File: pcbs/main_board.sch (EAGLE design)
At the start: 56 parts, among them IC1 317T, IC2 MEGA48/88/168-AU, J1 22-27-2021-02, K1 G6K-2F, Q1 MOSFET-NCHANNELSMD, Q2 MOSFET-NCHANNELSMD

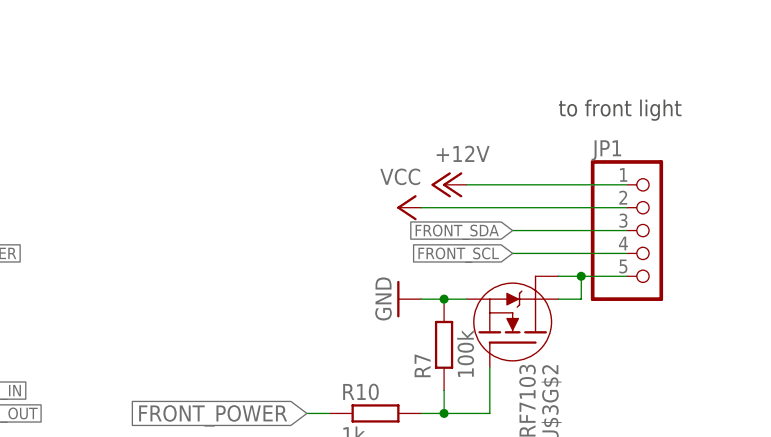
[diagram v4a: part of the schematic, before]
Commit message: Main Board: added i2c pullups.
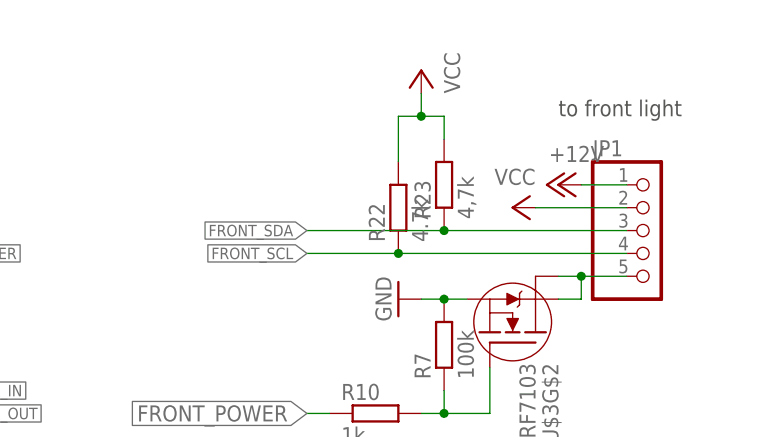
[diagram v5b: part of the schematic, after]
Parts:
- added R22: 4.7k, resistor:R-EU_R0805
- added R23: 4,7k, resistor:R-EU_R0805
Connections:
- net FRONT_SCL: now also R22.1
- net FRONT_SDA: now also R23.1
- net VCC: now also R22.2, R23.2
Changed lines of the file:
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@@
 <part name="R21" library="resistor" deviceset="R-EU_" device="R0805" value="1k"/>
 <part name="U$4" library="ShortCircuitRobotics" deviceset="IRF7413" device=""/>
+<part name="R22" library="resistor" deviceset="R-EU_" device="R0805" value="4.7k"/>
+<part name="R23" library="resistor" deviceset="R-EU_" device="R0805" value="4,7k"/>
+<part name="P+14" library="supply1" deviceset="VCC" device=""/>
 </parts>
 <sheets>
@@
 <instance part="JP2" gate="A" x="490.22" y="78.74"/>
 <instance part="GND6" gate="1" x="462.28" y="76.2" rot="R270"/>
-<instance part="P+5" gate="1" x="480.06" y="149.86" rot="MR270"/>
+<instance part="P+5" gate="1" x="492.76" y="149.86" rot="MR270"/>
 <instance part="P+6" gate="1" x="53.34" y="91.44"/>
 <instance part="Q1" gate="G$1" x="53.34" y="66.04"/>
@@
 <instance part="R10" gate="G$1" x="472.44" y="124.46"/>
 <instance part="P+8" gate="1" x="472.44" y="83.82" rot="MR270"/>
-<instance part="P+9" gate="VCC" x="474.98" y="147.32" rot="MR270"/>
+<instance part="P+9" gate="VCC" x="487.68" y="147.32" rot="MR270"/>
 <instance part="JP3" gate="G$1" x="439.42" y="99.06"/>
 <instance part="P+10" gate="VCC" x="454.66" y="101.6" rot="MR90"/>
@@
 <instance part="R21" gate="G$1" x="469.9" y="25.4"/>
 <instance part="U$4" gate="G$1" x="485.14" y="38.1" rot="MR90"/>
+<instance part="R22" gate="G$1" x="474.98" y="147.32" rot="R90"/>
+<instance part="R23" gate="G$1" x="480.06" y="149.86" rot="R90"/>
+<instance part="P+14" gate="VCC" x="477.52" y="162.56" rot="MR0"/>
 </instances>
 <busses>
@@
 <pinref part="JP1" gate="A" pin="1"/>
 <pinref part="P+5" gate="1" pin="+12V"/>
-<wire x1="482.6" y1="149.86" x2="500.38" y2="149.86" width="0.1524" layer="91"/>
+<wire x1="495.3" y1="149.86" x2="500.38" y2="149.86" width="0.1524" layer="91"/>
 </segment>
 <segment>
@@
 </segment>
 <segment>
-<wire x1="500.38" y1="147.32" x2="477.52" y2="147.32" width="0.1524" layer="91"/>
+<wire x1="500.38" y1="147.32" x2="490.22" y2="147.32" width="0.1524" layer="91"/>
 <pinref part="JP1" gate="A" pin="2"/>
 <pinref part="P+9" gate="VCC" pin="VCC"/>
@@
 <wire x1="439.42" y1="81.28" x2="447.04" y2="81.28" width="0.1524" layer="91"/>
 </segment>
+<segment>
+<pinref part="R22" gate="G$1" pin="2"/>
+<wire x1="474.98" y1="152.4" x2="474.98" y2="157.48" width="0.1524" layer="91"/>
+<pinref part="R23" gate="G$1" pin="2"/>
+<wire x1="474.98" y1="157.48" x2="477.52" y2="157.48" width="0.1524" layer="91"/>
+<wire x1="477.52" y1="157.48" x2="480.06" y2="157.48" width="0.1524" layer="91"/>
+<wire x1="480.06" y1="157.48" x2="480.06" y2="154.94" width="0.1524" layer="91"/>
+<wire x1="477.52" y1="157.48" x2="477.52" y2="160.02" width="0.1524" layer="91"/>
+<junction x="477.52" y="157.48"/>
+<pinref part="P+14" gate="VCC" pin="VCC"/>
+</segment>
 </net>
 <net name="FRONT_SDA" class="0">
 <segment>
-<wire x1="500.38" y1="144.78" x2="487.68" y2="144.78" width="0.1524" layer="91"/>
+<wire x1="500.38" y1="144.78" x2="480.06" y2="144.78" width="0.1524" layer="91"/>
 <pinref part="JP1" gate="A" pin="3"/>
-<label x="487.68" y="144.78" size="1.27" layer="95" rot="R180" xref="yes"/>
+<label x="464.82" y="144.78" size="1.27" layer="95" rot="R180" xref="yes"/>
+<pinref part="R23" gate="G$1" pin="1"/>
+<wire x1="480.06" y1="144.78" x2="464.82" y2="144.78" width="0.1524" layer="91"/>
+<junction x="480.06" y="144.78"/>
 </segment>
 <segment>
@@
 <net name="FRONT_SCL" class="0">
 <segment>
-<wire x1="500.38" y1="142.24" x2="487.68" y2="142.24" width="0.1524" layer="91"/>
+<wire x1="500.38" y1="142.24" x2="474.98" y2="142.24" width="0.1524" layer="91"/>
 <pinref part="JP1" gate="A" pin="4"/>
-<label x="487.68" y="142.24" size="1.27" layer="95" rot="R180" xref="yes"/>
-</segment>
-<segment>
+<label x="464.82" y="142.24" size="1.27" layer="95" rot="R180" xref="yes"/>
+<pinref part="R22" gate="G$1" pin="1"/>
+<wire x1="474.98" y1="142.24" x2="464.82" y2="142.24" width="0.1524" layer="91"/>
+<junction x="474.98" y="142.24"/>
+</segment>
+<segment>

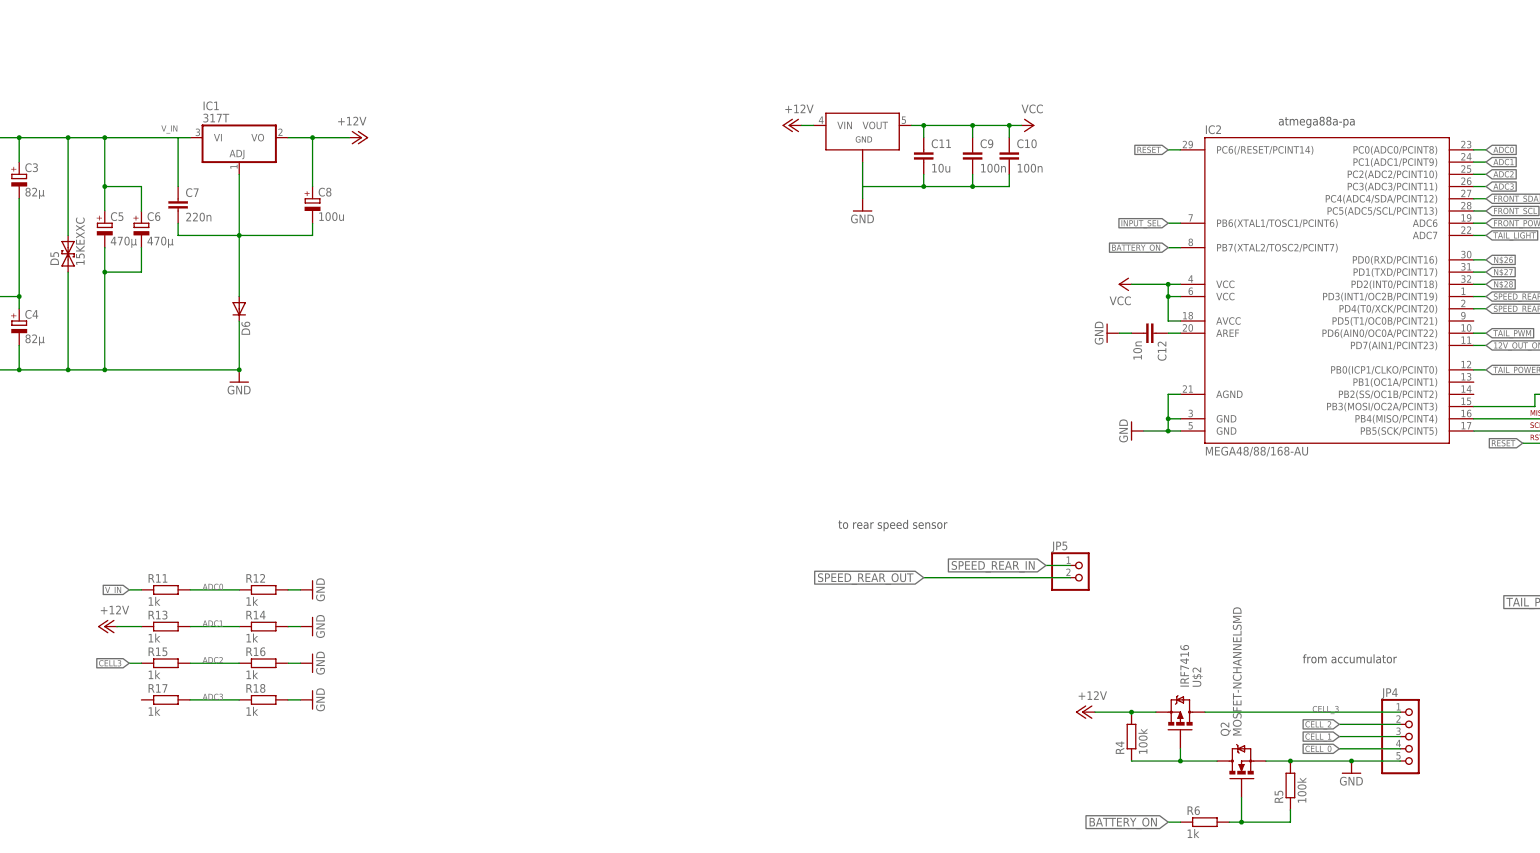
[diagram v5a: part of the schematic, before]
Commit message: Main Board: Changed battery connection.
It does not make sense to disconnect the battery from the uC....
Instead it makes sense to disconnect the charging/input circuit
when the battery is full and disconnect the peripherals when it is
getting empty.
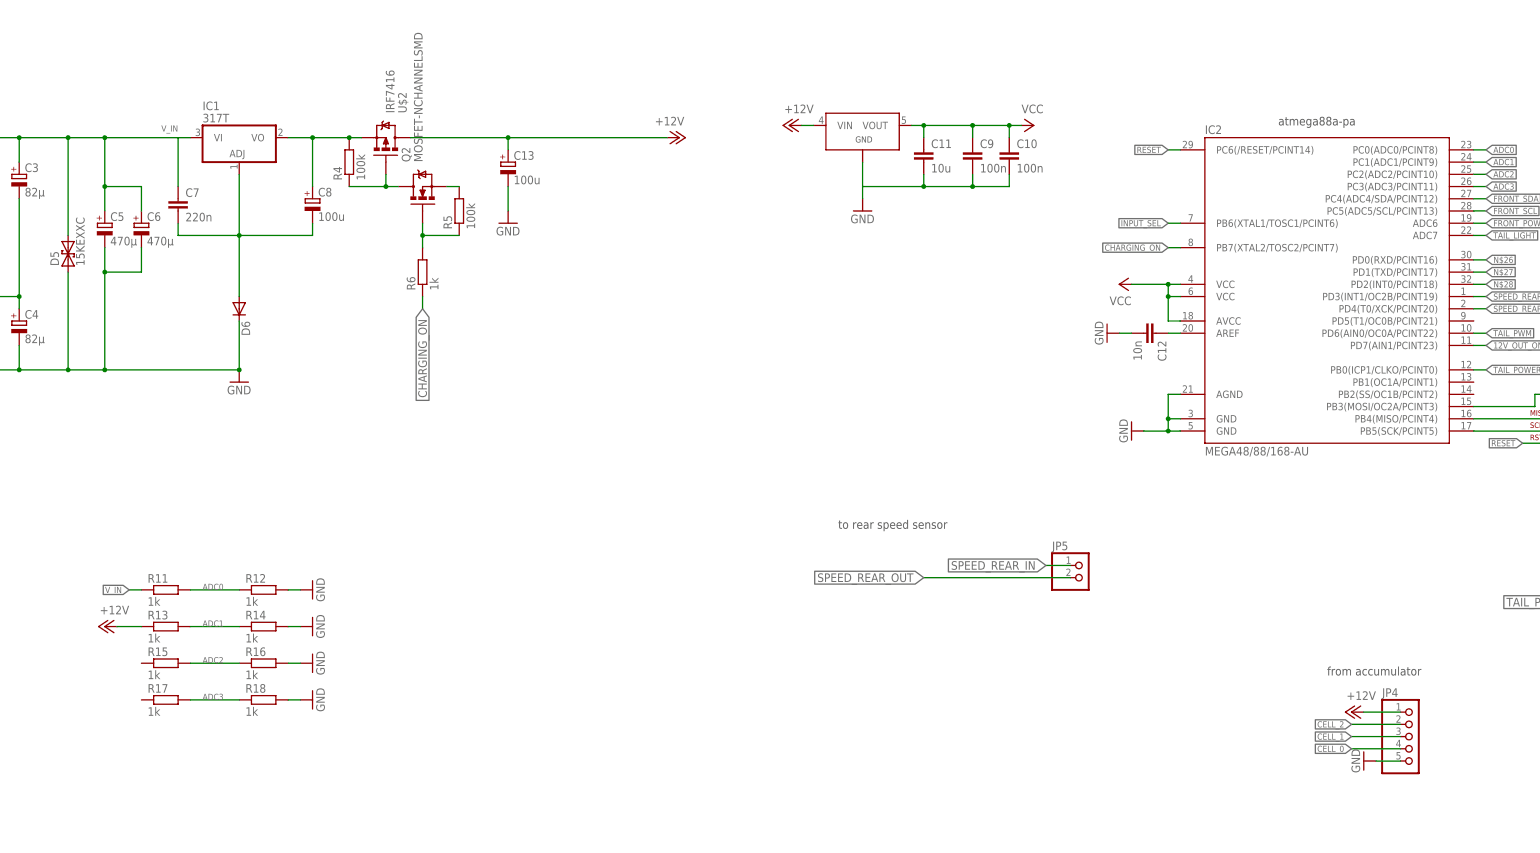
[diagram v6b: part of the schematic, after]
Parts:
- added C13: 100u, resistor:CPOL-EUE
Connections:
- net BATTERY_ON renamed CHARGING_ON
- removed net CELL3: R15.1
- removed net CELL_3: JP4.1, U$2.D1
- new net N$23: Q2.S, R5.2
- new net N$24: C8.+, IC1.VO, R4.2, U$2.S1
- net +12V: now also C13.+, JP4.1, U$2.D1; no longer C8.+, IC1.VO, R4.2, U$2.S1
- net GND: now also C13.-; no longer Q2.S, R5.2
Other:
- moved on the sheet: Q2, R4, R5, R6, U$2

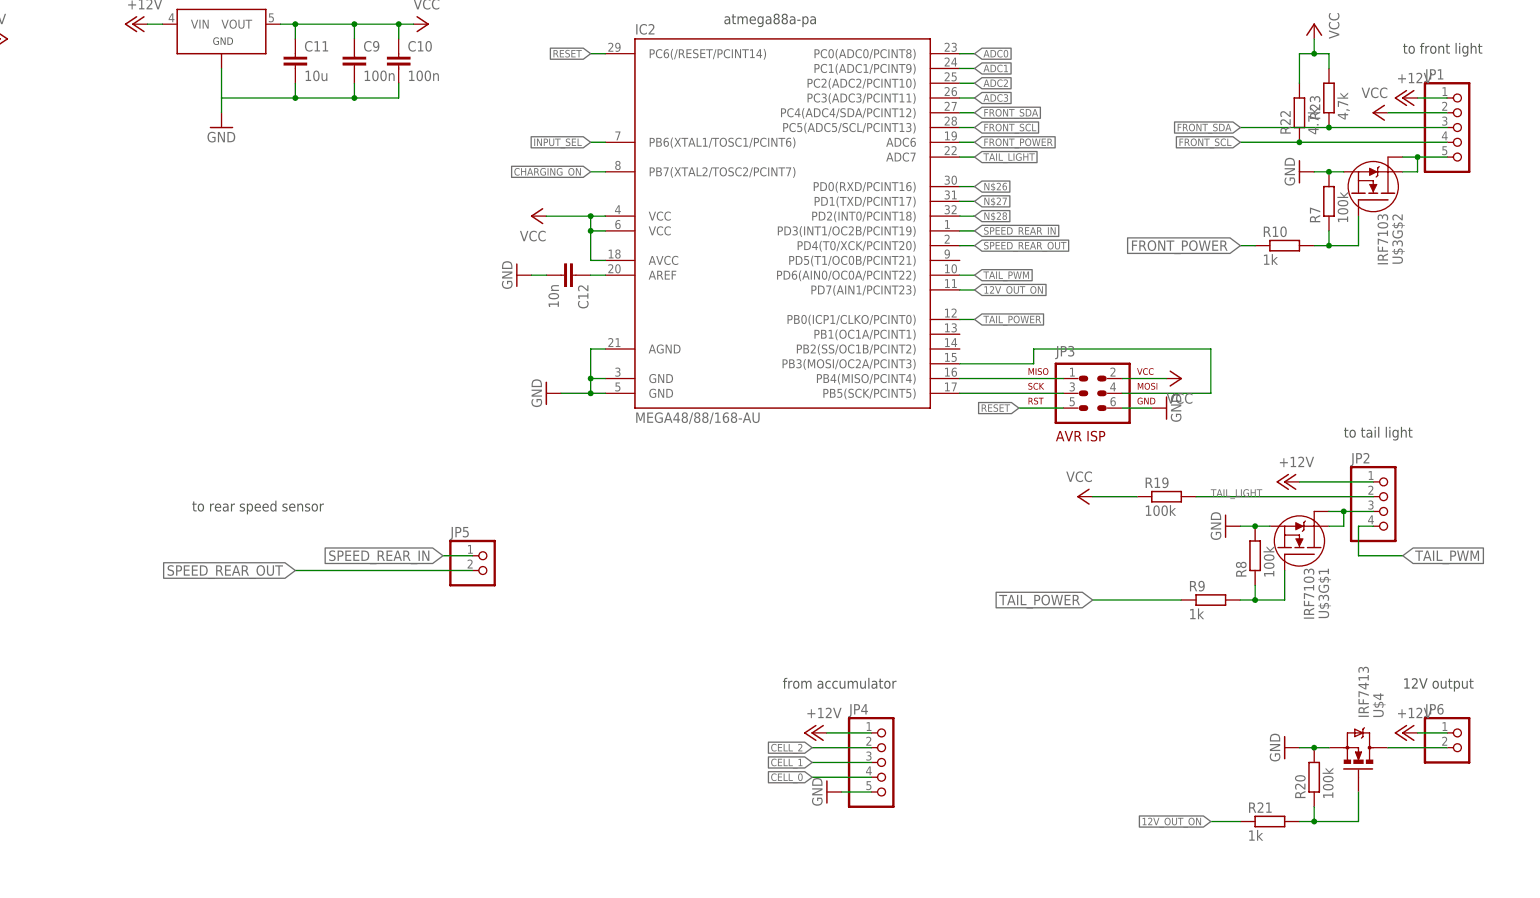
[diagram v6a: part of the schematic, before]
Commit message: Main Board: Added back i2c
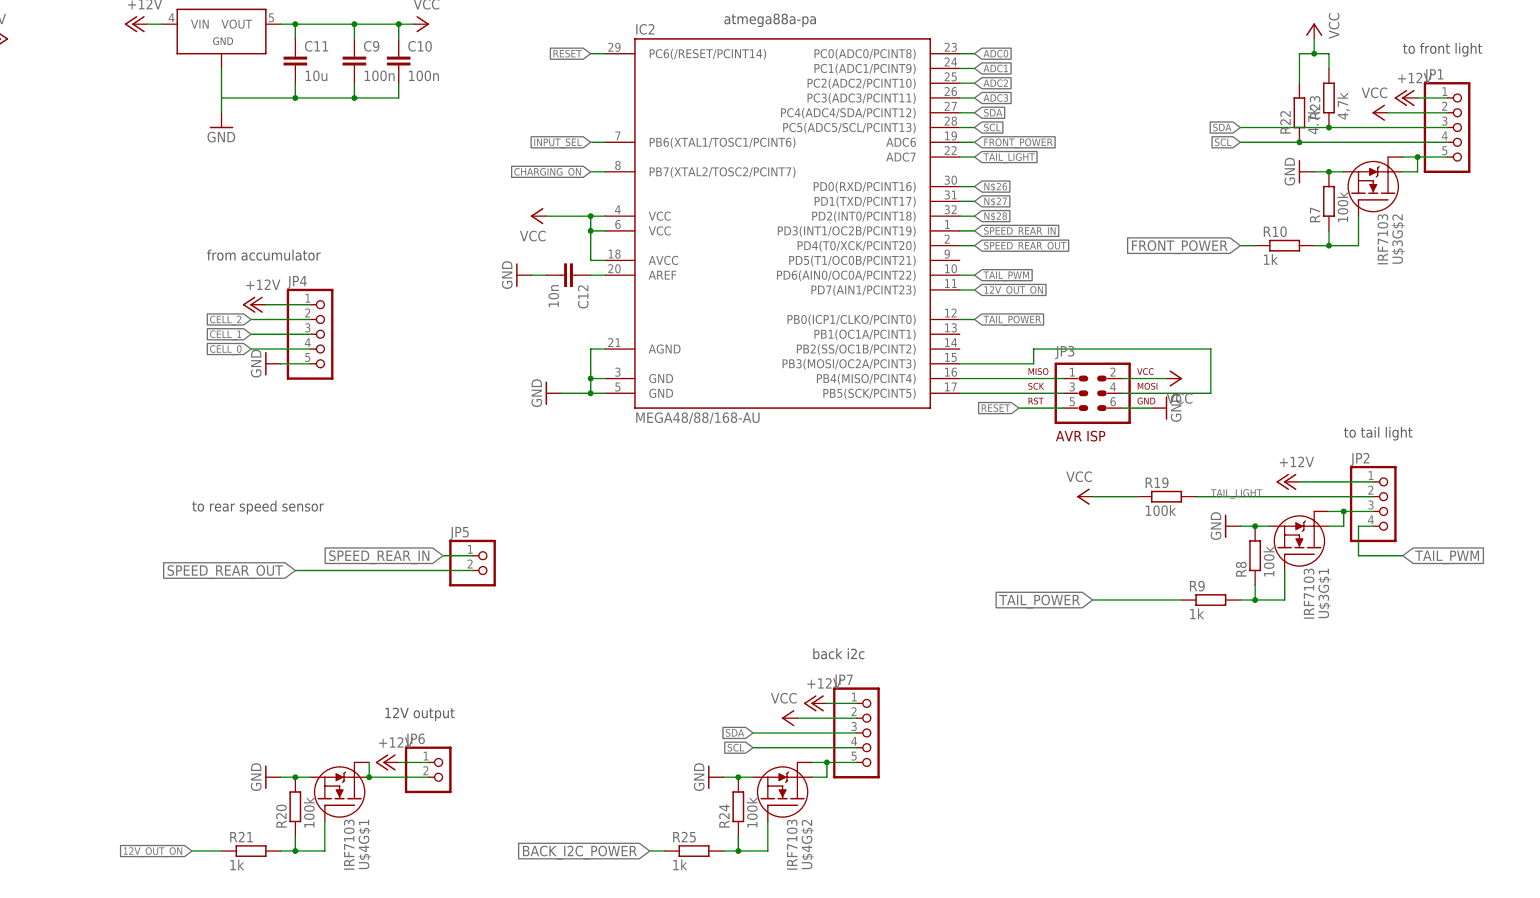
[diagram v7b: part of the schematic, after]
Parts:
- added JP7: (no value), pinhead:PINHD-1X5
- added R24: 100k, resistor:R-EU_R0805
- added R25: 1k, resistor:R-EU_R0805
- U$4: value IRF7413 -> IRF7103; device ShortCircuitRobotics:IRF7413 -> irf-2:IRF7103
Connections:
- removed net FRONT_SCL: IC2.PC5(ADC5/SCL/PCINT13), JP1.4, R22.1
- removed net FRONT_SDA: IC2.PC4(ADC4/SDA/PCINT12), JP1.3, R23.1
- new net BACK_I2C_POWER: R25.1
- new net N$25: JP7.5, U$4G$2.D@1, U$4G$2.D@2
- new net N$29: R24.1, R25.2, U$4G$2.G
- new net SCL: IC2.PC5(ADC5/SCL/PCINT13), JP1.4, JP7.4, R22.1
- new net SDA: IC2.PC4(ADC4/SDA/PCINT12), JP1.3, JP7.3, R23.1
- net +12V: now also JP7.1
- net GND: now also R24.2, U$4G$1.S, U$4G$2.S; no longer U$4.S1
- net N$22: now also U$4G$1.G; no longer U$4.G
- net N$5: now also U$4G$1.D@1, U$4G$1.D@2; no longer U$4.D1
- net VCC: now also JP7.2
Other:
- note added: "back i2c"
- moved on the sheet: JP4, JP6, R20, R21
